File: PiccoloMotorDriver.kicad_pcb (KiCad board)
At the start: 6 copper layers, 68 x 68 mm, 152 parts, among them J1 Conn_01x06_SWD, J10 AUX2, J11 C189893, J12 Conn_01x01, J13 Conn_01x01, J2 Conn_01x01, J3 C189893, J4 C225127, J5 Screw_Terminal_01x02_POWER, J6 Connector, USB-TYPE-C-16P, J7 C225127, J8 AUX0, J9 AUX1, Q1 NE006NG, Q2 NE006NG, Q3 NE006NG, Q4 NE006NG, Q5 NE006NG, Q7 NE006NG, U1 SP485EEN, U12 STM32H723VGT6, U2 XC6210B332MR, U3 XL1509, U4 TJA1050T/CM,118, U5 AS5047D, U6 USBLC6-2SC6, U7 DRV8353SRTAR, X2 X322516MLB4SI

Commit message: Placement, some layout
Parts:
- removed C47, C48, C49: 100nF, PCM_JLCPCB:C_0603
- removed R25, R40, R42: 47kΩ, PCM_JLCPCB:R_0603
- removed R34, R41, R43: 1kΩ, PCM_JLCPCB:R_0603
- added SW1: SW_DIP_x02, Package_DIP:SMDIP-4_W7.62mm, F.Cu at (149.4, 115.6)
- added U8: AS5047D, Package_SO:TSSOP-14_4.4x5mm_P0.65mm, F.Cu at (159.0, 116.1)
- moved R26 80.9 mm to (114.2, 114.3)
- moved FB2 73.2 mm to (122.0, 98.7), turned to 180 degrees
- moved R63 65.4 mm to (125.5, 96.1), turned to 90 degrees
- moved J7 64.3 mm to (134.8, 126.7), turned to -6 degrees
- moved R62 63.5 mm to (127.0, 96.1), turned to 90 degrees
- moved R61 61.6 mm to (128.5, 96.1), turned to 90 degrees
- moved J1 51.5 mm to (145.0, 125.9), turned to 13 degrees
- moved C21 48.5 mm to (165.5, 91.0), turned to -90 degrees
- moved J4 47.2 mm to (113.0, 130.1), turned to -45 degrees
- moved R36 47.0 mm to (105.6, 132.9)
- moved C22 46.0 mm to (157.2, 99.5), turned to 90 degrees
- moved C6 45.4 mm to (128.5, 98.9), turned to -90 degrees
- moved C23 45.0 mm to (163.7, 101.2)
- moved R35 44.7 mm to (110.1, 133.1)
- moved D1 43.9 mm to (101.4, 133.2)
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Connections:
- R14 pad 1: ~{DRV_FAULT} -> Net-(U7-FAULT_N)
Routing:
- net Net-(U7-SDI): track 0.00 -> 57.8 mm, vias 0 -> 2
- net Net-(U7-SCLK): track 0.00 -> 53.2 mm, vias 0 -> 2
- net Net-(U7-INLB): track 0.00 -> 52.4 mm, vias 0 -> 2
- net Net-(U7-SCS_N): track 0.00 -> 48.3 mm, vias 0 -> 2
- net Net-(U7-INHB): track 0.00 -> 48.0 mm, vias 0 -> 2
- net Net-(U7-INHC): track 0.00 -> 47.7 mm, vias 0 -> 2
- net Net-(U7-INLC): track 0.00 -> 47.6 mm, vias 0 -> 2
- net Net-(U7-ENABLE): track 0.00 -> 42.4 mm, vias 0 -> 2
- net Net-(U7-SDO): track 0.00 -> 40.1 mm, vias 0 -> 2
- net /Inverter/PHASE_C: track 0.00 -> 39.8 mm, vias 0 -> 65
- net Net-(U7-INLA): track 0.00 -> 38.6 mm, vias 0 -> 2
- net Net-(U7-INHA): track 0.00 -> 36.7 mm, vias 0 -> 2
- net Net-(U7-SOC): track 0.00 -> 34.2 mm, vias 0 -> 2
- net Net-(U7-SOB): track 0.00 -> 31.4 mm, vias 0 -> 2
- net Net-(U7-GLC): track 0.00 -> 30.8 mm, vias 0 -> 2
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- added copper zone on F.Cu, net /Inverter/PHASE_A
- added copper zone on F.Cu, net /Inverter/PHASE_B
- added copper zone on F.Cu, net /Inverter/PHASE_C
- added copper zone on F.Cu, net Net-(U7-SPA)
- added copper zone on F.Cu, net Net-(U7-SPB)
- added copper zone on F.Cu, net Net-(U7-SPC)
- added copper zone on B.Cu, net Vdrive
- added copper zone on In2.Cu, net Vdrive

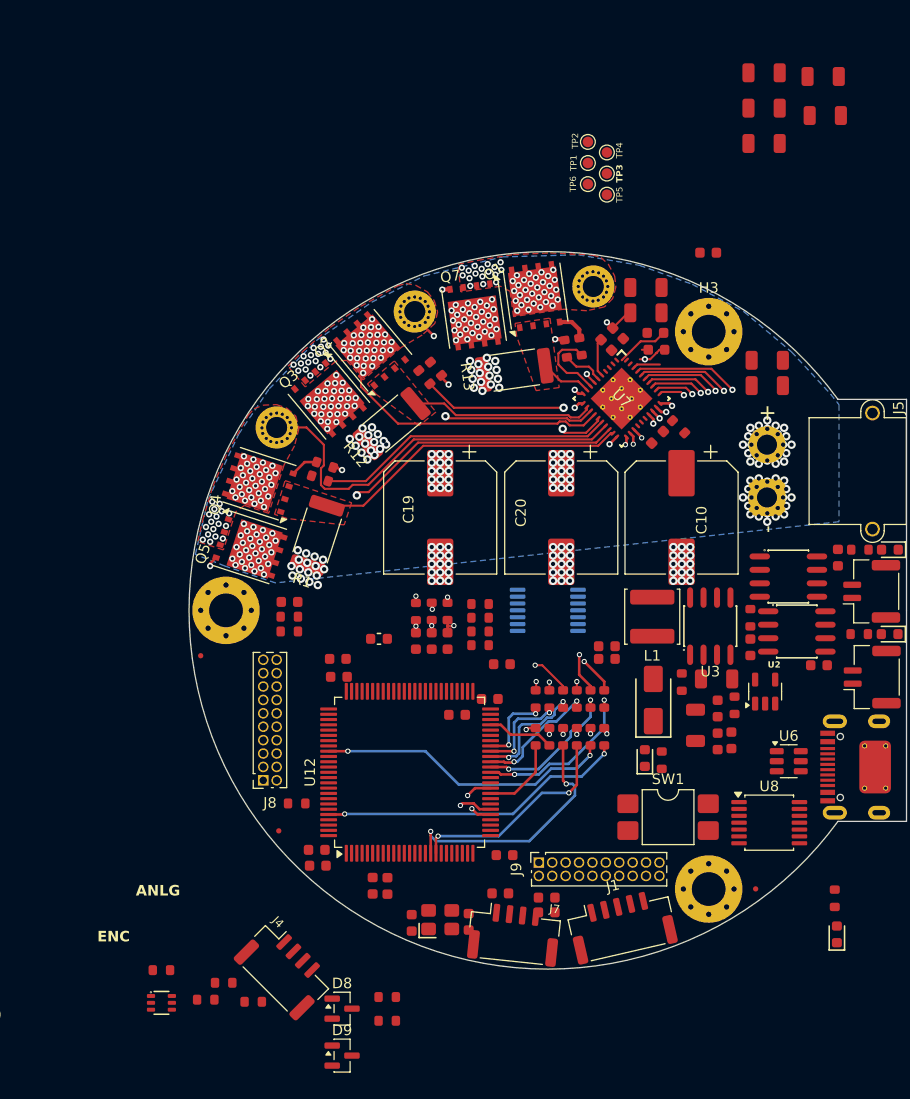
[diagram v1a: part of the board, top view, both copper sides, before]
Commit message: Reduced number of 10uF caps
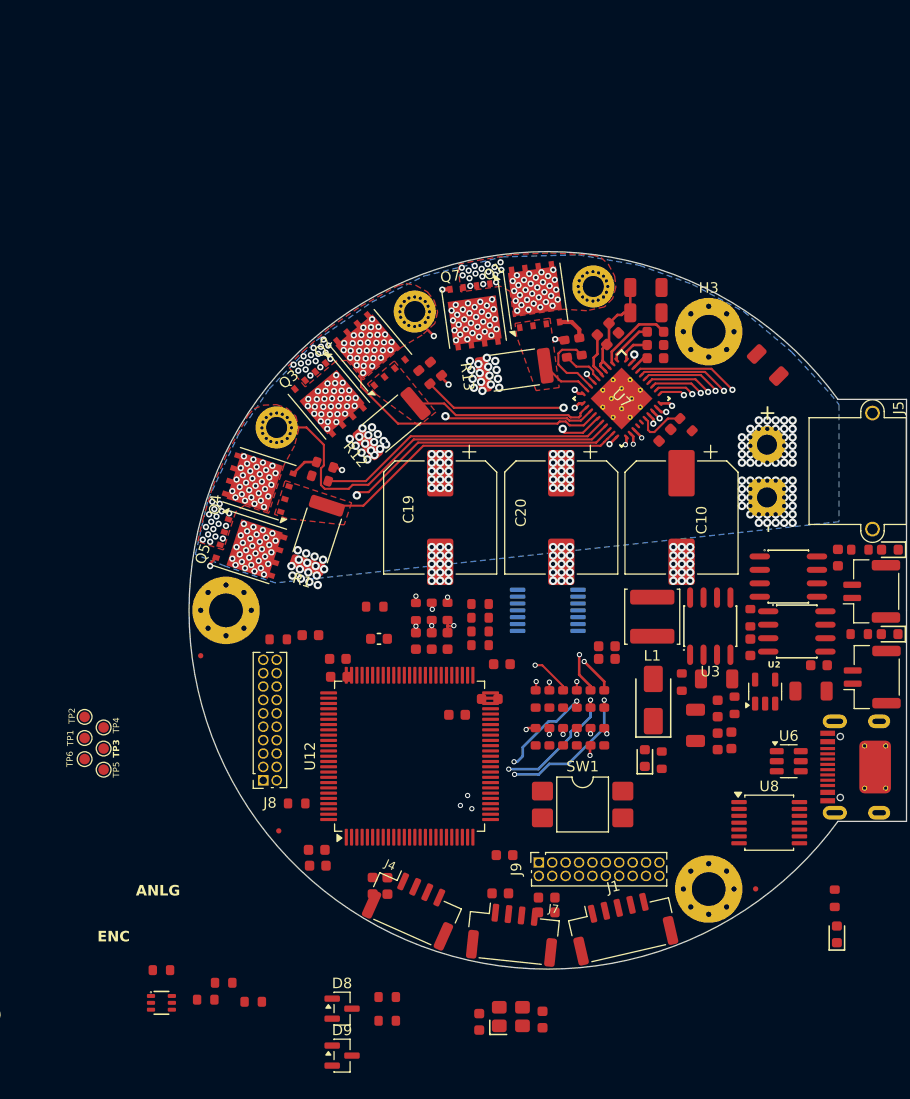
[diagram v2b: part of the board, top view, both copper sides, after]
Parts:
- removed C40, C41, C42, C43, C44: 10uF, PCM_JLCPCB:C_1206
- moved TP1 72.4 mm to (94.1, 108.1)
- moved TP2 72.4 mm to (94.1, 106.1)
- moved TP6 72.4 mm to (94.1, 110.1)
- moved TP3 72.4 mm to (95.9, 109.1)
- moved TP4 72.4 mm to (95.9, 107.1)
- moved TP5 72.4 mm to (95.9, 111.1)
- moved C7 58.8 mm to (162.9, 103.7)
- moved J4 13.6 mm to (125.2, 124.2), turned to -24 degrees
- moved C9 11.6 mm to (137.5, 134.8)
- moved X2 11.4 mm to (134.5, 134.5)
- moved C8 11.4 mm to (131.5, 135.0)
- moved C54 11.2 mm to (148.2, 72.1)
- moved SW1 8.19 mm to (141.3, 114.4)
- moved R64 8.16 mm to (121.6, 95.7)
- moved C16 3.72 mm to (115.5, 98.3)
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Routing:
- net DRV_SPI_~{SCS}: track 29.3 -> 0.00 mm, vias 2 -> 0
- net DRV_SPI_CLK: track 28.2 -> 0.97 mm, vias 2 -> 1
- net DRV_SPI_SDO: track 23.7 -> 0.00 mm, vias 2 -> 0
- net DRV_SPI_SDI: track 20.6 -> 0.00 mm, vias 2 -> 0
- net PWM_B_H: track 11.4 -> 0.00 mm, vias 2 -> 0
- net PWM_C_L: track 9.15 -> 0.00 mm, vias 2 -> 0
- net Vdrive: track 3.05 -> 10.8 mm, vias 150 -> 156
- net ~{DRV_FAULT}: track 7.65 -> 0.00 mm
- net PWM_C_H: track 7.61 -> 0.00 mm, vias 2 -> 0
- net Net-(U7-CPH): track 0.00 -> 7.48 mm
- net DRV_OFF: track 6.38 -> 0.00 mm
- net Net-(U7-FAULT_N): track 0.96 -> 5.81 mm
- net AN_DRV_SO_B: track 23.1 -> 19.9 mm
- net AN_DRV_SO_C: track 21.2 -> 18.7 mm
- net Net-(U7-VGLS): track 0.60 -> 3.02 mm
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
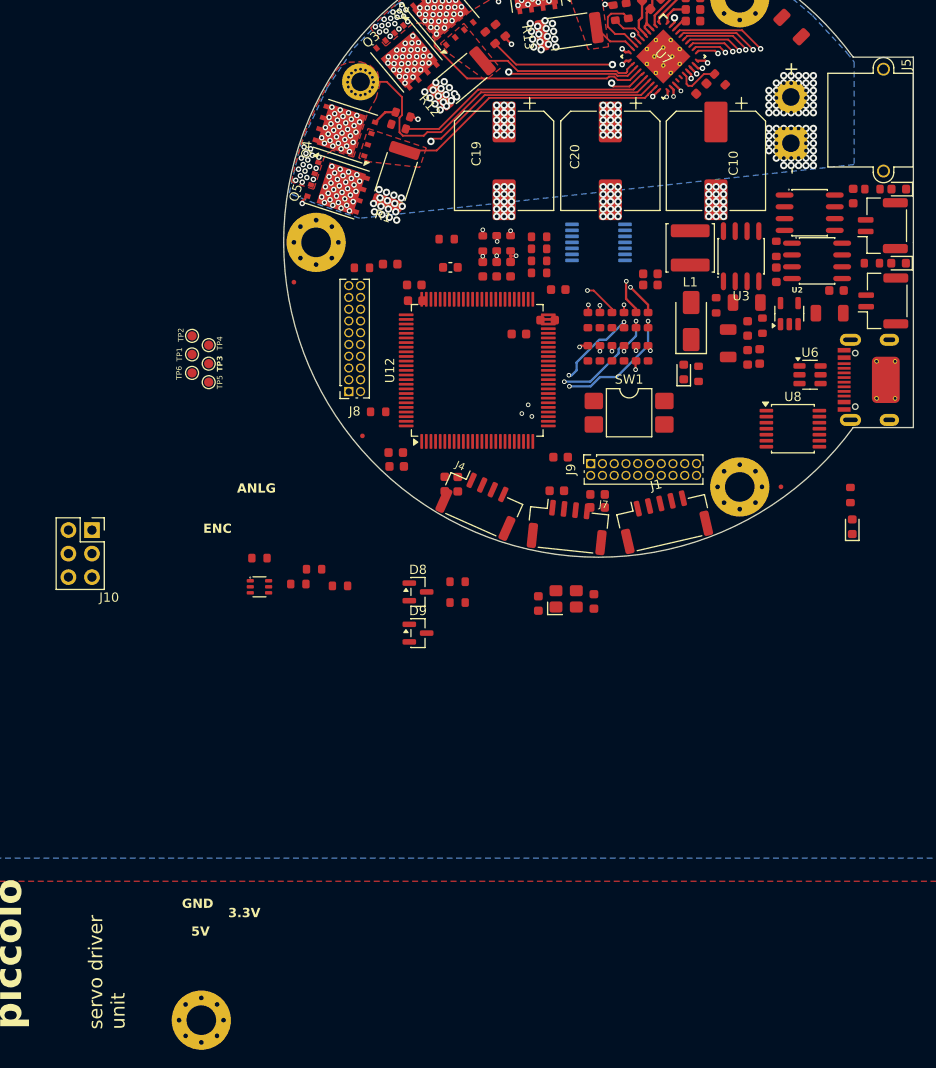
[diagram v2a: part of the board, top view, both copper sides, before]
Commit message: More layout, add can,rs485 leds
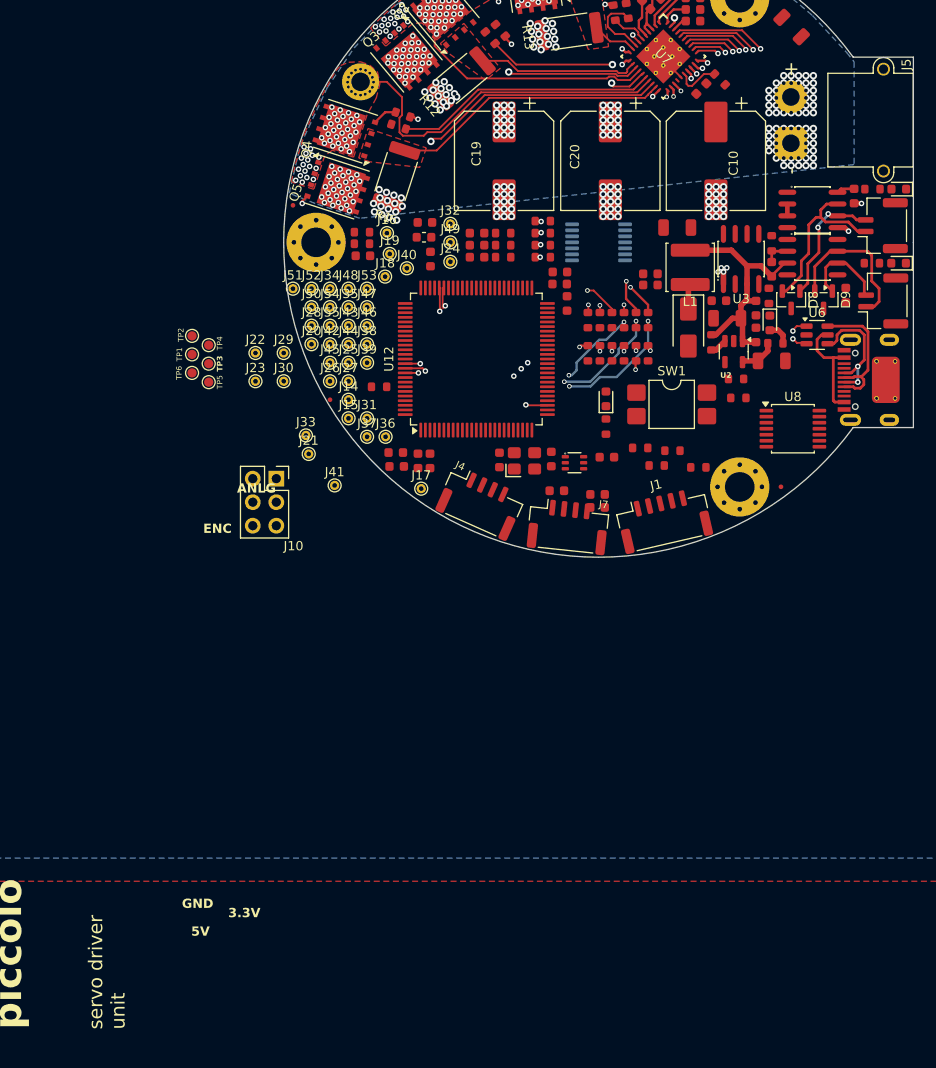
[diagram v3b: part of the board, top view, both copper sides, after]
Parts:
- removed H1: MountingHole_Pad, MountingHole:MountingHole_3.2mm_M3_Pad_Via
- removed J8: AUX0, Connector_PinSocket_1.27mm:PinSocket_2x10_P1.27mm_Vertical
- removed J9: AUX1, Connector_PinSocket_1.27mm:PinSocket_2x10_P1.27mm_Vertical
- added J14: IO, TestPoint:TestPoint_THTPad_D1.0mm_Drill0.5mm, F.Cu at (111.0, 113.0)
- added J15: IO, TestPoint:TestPoint_THTPad_D1.0mm_Drill0.5mm, F.Cu at (111.0, 115.0)
- added J16: IO, TestPoint:TestPoint_THTPad_D1.0mm_Drill0.5mm, F.Cu at (115.2, 95.0)
- added J17: IO, TestPoint:TestPoint_THTPad_D1.0mm_Drill0.5mm, F.Cu at (118.8, 122.6)
- added J18: IO, TestPoint:TestPoint_THTPad_D1.0mm_Drill0.5mm, F.Cu at (115.0, 99.7)
- added J19: IO, TestPoint:TestPoint_THTPad_D1.0mm_Drill0.5mm, F.Cu at (115.5, 97.2)
- added J20: IO, TestPoint:TestPoint_THTPad_D1.0mm_Drill0.5mm, F.Cu at (107.0, 107.0)
- added J21: IO, TestPoint:TestPoint_THTPad_D1.0mm_Drill0.5mm, F.Cu at (106.7, 118.8)
- added J22: IO, TestPoint:TestPoint_THTPad_D1.0mm_Drill0.5mm, F.Cu at (101.0, 108.0)
- added J23: IO, TestPoint:TestPoint_THTPad_D1.0mm_Drill0.5mm, F.Cu at (101.0, 111.0)
- added J24: IO, TestPoint:TestPoint_THTPad_D1.0mm_Drill0.5mm, F.Cu at (122.0, 98.1)
- added J25: IO, TestPoint:TestPoint_THTPad_D1.0mm_Drill0.5mm, F.Cu at (111.0, 109.0)
- added J26: IO, TestPoint:TestPoint_THTPad_D1.0mm_Drill0.5mm, F.Cu at (109.0, 111.0)
- added J27: IO, TestPoint:TestPoint_THTPad_D1.0mm_Drill0.5mm, F.Cu at (111.0, 111.0)
- added J28: IO, TestPoint:TestPoint_THTPad_D1.0mm_Drill0.5mm, F.Cu at (107.0, 105.0)
- added J29: IO, TestPoint:TestPoint_THTPad_D1.0mm_Drill0.5mm, F.Cu at (104.0, 108.0)
- added J30: IO, TestPoint:TestPoint_THTPad_D1.0mm_Drill0.5mm, F.Cu at (104.0, 111.0)
- added J31: IO, TestPoint:TestPoint_THTPad_D1.0mm_Drill0.5mm, F.Cu at (113.0, 115.0)
- added J32: IO, TestPoint:TestPoint_THTPad_D1.0mm_Drill0.5mm, F.Cu at (122.0, 94.0)
- added J33: IO, TestPoint:TestPoint_THTPad_D1.0mm_Drill0.5mm, F.Cu at (106.4, 116.8)
- added J34: IO, TestPoint:TestPoint_THTPad_D1.0mm_Drill0.5mm, F.Cu at (109.0, 101.0)
- added J35: IO, TestPoint:TestPoint_THTPad_D1.0mm_Drill0.5mm, F.Cu at (111.0, 103.0)
- added J36: IO, TestPoint:TestPoint_THTPad_D1.0mm_Drill0.5mm, F.Cu at (115.0, 117.0)
- added J37: IO, TestPoint:TestPoint_THTPad_D1.0mm_Drill0.5mm, F.Cu at (113.0, 117.0)
- added J38: IO, TestPoint:TestPoint_THTPad_D1.0mm_Drill0.5mm, F.Cu at (113.0, 107.0)
- added J39: IO, TestPoint:TestPoint_THTPad_D1.0mm_Drill0.5mm, F.Cu at (113.0, 109.0)
- added J40: IO, TestPoint:TestPoint_THTPad_D1.0mm_Drill0.5mm, F.Cu at (117.3, 98.8)
- added J41: IO, TestPoint:TestPoint_THTPad_D1.0mm_Drill0.5mm, F.Cu at (109.5, 122.2)
- added J42: IO, TestPoint:TestPoint_THTPad_D1.0mm_Drill0.5mm, F.Cu at (109.0, 107.0)
- added J43: IO, TestPoint:TestPoint_THTPad_D1.0mm_Drill0.5mm, F.Cu at (111.0, 105.0)
- added J44: IO, TestPoint:TestPoint_THTPad_D1.0mm_Drill0.5mm, F.Cu at (111.0, 107.0)
- added J45: IO, TestPoint:TestPoint_THTPad_D1.0mm_Drill0.5mm, F.Cu at (109.0, 109.0)
- added J46: IO, TestPoint:TestPoint_THTPad_D1.0mm_Drill0.5mm, F.Cu at (113.0, 105.0)
- added J47: IO, TestPoint:TestPoint_THTPad_D1.0mm_Drill0.5mm, F.Cu at (113.0, 103.0)
- added J48: IO, TestPoint:TestPoint_THTPad_D1.0mm_Drill0.5mm, F.Cu at (111.0, 101.0)
- added J49: IO, TestPoint:TestPoint_THTPad_D1.0mm_Drill0.5mm, F.Cu at (122.0, 96.0)
- added J50: IO, TestPoint:TestPoint_THTPad_D1.0mm_Drill0.5mm, F.Cu at (107.0, 103.0)
- added J51: IO, TestPoint:TestPoint_THTPad_D1.0mm_Drill0.5mm, F.Cu at (105.0, 101.0)
- added J52: IO, TestPoint:TestPoint_THTPad_D1.0mm_Drill0.5mm, F.Cu at (107.0, 101.0)
- added J53: IO, TestPoint:TestPoint_THTPad_D1.0mm_Drill0.5mm, F.Cu at (113.0, 101.0)
- added J54: IO, TestPoint:TestPoint_THTPad_D1.0mm_Drill0.5mm, F.Cu at (109.0, 103.0)
- added J55: IO, TestPoint:TestPoint_THTPad_D1.0mm_Drill0.5mm, F.Cu at (109.0, 105.0)
- moved D9 56.7 mm to (162.3, 102.2), turned to -90 degrees
- moved D8 51.2 mm to (158.8, 102.2), turned to -90 degrees
- moved R33 42.8 mm to (142.5, 118.2)
- moved R35 40.8 mm to (148.8, 120.3)
- moved R36 40.8 mm to (144.3, 120.1)
- moved R30 40.8 mm to (146.0, 118.5)
- moved R22 37.5 mm to (153.1, 112.8)
- moved R8 37.2 mm to (152.8, 110.8)
- moved D1 36.6 mm to (135.4, 119.8)
- moved D4 30.0 mm to (138.8, 112.9)
- moved R38 27.4 mm to (138.8, 115.9)
- moved J10 20.7 mm to (103.2, 121.5)
- moved C7 18.9 mm to (146.5, 94.4), turned to 180 degrees
- moved C8 16.1 mm to (127.3, 119.5)
- moved C9 16.1 mm to (132.9, 119.4)
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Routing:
- net USB+: track 0.00 -> 44.1 mm, vias 0 -> 2
- net USB-: track 0.00 -> 43.7 mm, vias 0 -> 2
- net ENC_MOSI: track 0.00 -> 30.5 mm, vias 0 -> 3
- net +5V: track 0.00 -> 29.2 mm
- net ENC_MISO: track 0.00 -> 29.0 mm, vias 0 -> 3
- net ENC_CLK: track 0.00 -> 27.2 mm, vias 0 -> 3
- net AN_DRV_SO_A: track 19.9 -> 0.00 mm, vias 2 -> 0
- net AN_DRV_SO_B: track 19.9 -> 0.00 mm, vias 2 -> 0
- net ENC_CS: track 0.00 -> 19.5 mm, vias 0 -> 2
- net AN_DRV_SO_C: track 18.7 -> 0.00 mm, vias 2 -> 0
- net /IO/RS485-: track 0.00 -> 18.6 mm
- net /IO/CAN+: track 0.00 -> 16.6 mm
- net Net-(J6-D--PadA7): track 0.00 -> 15.0 mm
- net /IO/RS485+: track 0.00 -> 14.0 mm, vias 0 -> 2
- net Net-(J6-D+-PadA6): track 0.00 -> 13.8 mm, vias 0 -> 2
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
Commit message: Deleted some parts to fit inside the pcb area. Layout
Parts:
- moved C12 0.64 mm to (125.4, 94.6)
- moved C11 0.64 mm to (125.4, 95.9)
- moved C6 0.64 mm to (125.4, 97.2)
- moved R63 0.64 mm to (128.2, 94.6)
- moved R61 0.64 mm to (128.2, 97.2)
- moved R62 0.64 mm to (128.2, 95.9)
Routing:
- net CAN_RX: track 0.00 -> 60.8 mm, vias 0 -> 3
- net RS485_DI: track 0.00 -> 60.5 mm, vias 0 -> 3
- net RS485_RO: track 0.00 -> 59.2 mm, vias 0 -> 3
- net RS485_DE: track 1.28 -> 56.9 mm, vias 0 -> 3
- net CAN_TX: track 0.00 -> 53.0 mm, vias 0 -> 3
- net DRV_SPI_~{SCS}: track 0.00 -> 26.9 mm, vias 0 -> 2
- net DRV_SPI_CLK: track 0.97 -> 26.0 mm, vias 1 -> 2
- net AN_DRV_SO_B: track 0.00 -> 24.0 mm, vias 0 -> 2
- net AN_DRV_SO_A: track 0.00 -> 22.4 mm, vias 0 -> 2
- net AN_DRV_SO_C: track 0.00 -> 21.9 mm, vias 0 -> 2
- net DRV_SPI_SDI: track 0.00 -> 15.0 mm, vias 0 -> 1
- net DRV_SPI_SDO: track 0.00 -> 14.6 mm, vias 0 -> 1
- net PWM_B_H: track 0.00 -> 7.75 mm
- net Net-(U5-MISO): track 0.00 -> 6.55 mm, vias 0 -> 1
- net PWM_C_L: track 0.00 -> 6.25 mm
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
